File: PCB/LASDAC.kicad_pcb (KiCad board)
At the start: 2 copper layers, 110 x 70 mm, 91 parts, among them P1 USB_B, P2 CONN_01X25, U1 Mounting_Hole, U10 TL084_v, U11 LM358, U12 TL084_v, U2 Mounting_Hole, U3 Mounting_Hole, U4 Mounting_Hole, U5 AP2114, U6 SPX431, U7 ISA_DC-DC_converter, U8 ATSAM4S, U9 DAC084S085C, Y1 12MHz .25%

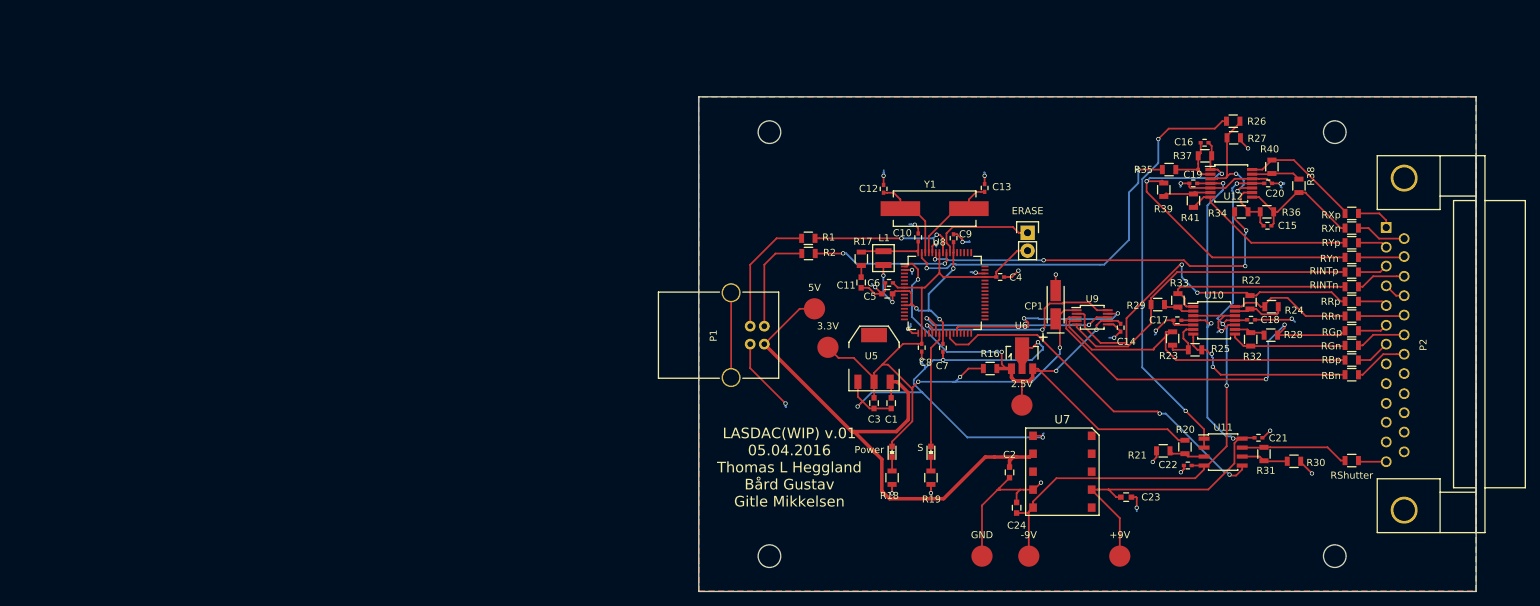
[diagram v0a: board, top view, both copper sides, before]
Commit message: Generated BOM, fixed component names in schematic
Changed component names on output resistors and status LED to match that
in PCB
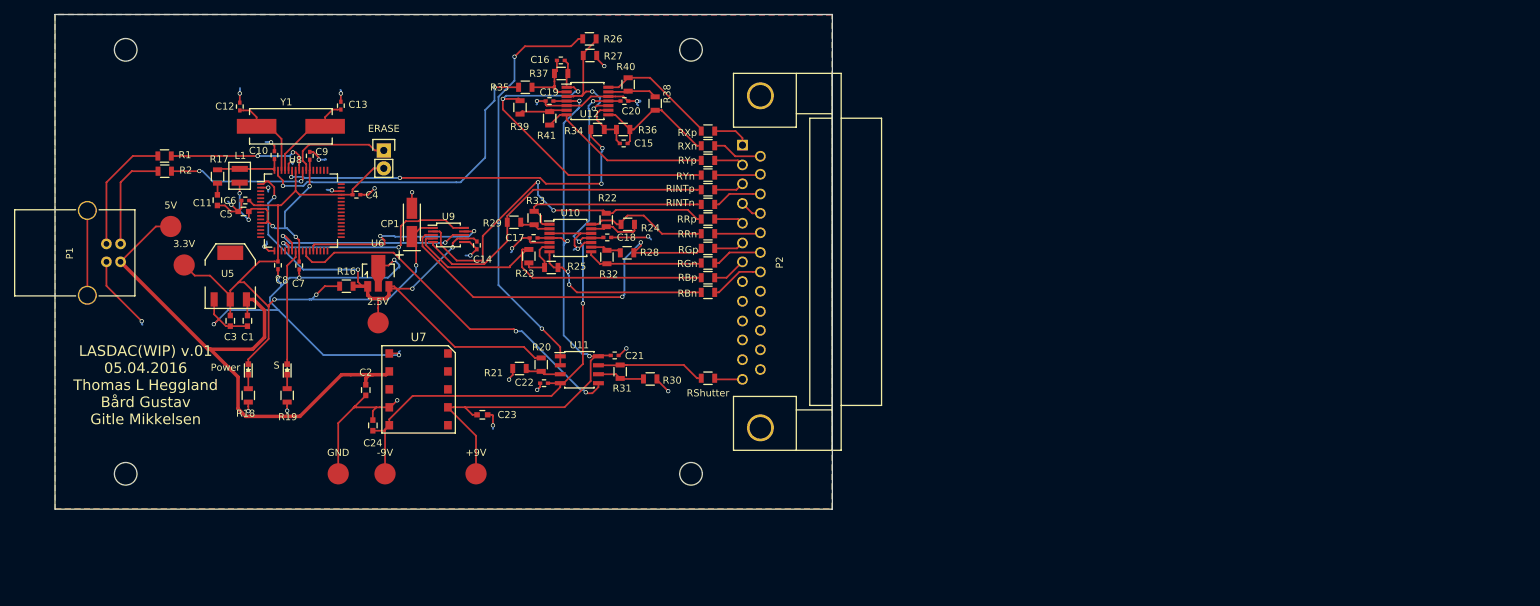
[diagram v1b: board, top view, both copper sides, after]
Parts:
- moved P2 91.8 mm to (167.4, 83.3)
- moved R20 91.8 mm to (137.7, 97.9)
- moved R23 91.8 mm to (135.9, 82.5)
- moved R24 91.8 mm to (149.9, 78.0)
- moved R33 91.8 mm to (136.7, 77.2)
- moved R35 91.8 mm to (135.4, 58.6)
- moved R38 91.8 mm to (153.8, 61.0)
- moved R39 91.8 mm to (134.7, 61.5)
- moved U10 91.8 mm to (141.8, 80.0)
- moved 3.3V 91.8 mm to (87.2, 83.8)
- moved C10 91.8 mm to (100.0, 68.2)
- moved C12 91.8 mm to (95.0, 61.4)
- moved C3 91.8 mm to (93.7, 91.7)
- moved C4 91.8 mm to (111.5, 73.8)
- moved C5 91.8 mm to (95.6, 76.2)
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
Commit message: Reannotated Components
Annotated components to standards,
TODO: Add Silkscreen for signals on bottom
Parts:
- R16: value 1R -> 330R
- renumbered +9V to +9V1, -9V to -9V1, 2.5V to 2.5V1, 3.3V to 3.3V1, 5V to 5V1, C9 to C10, C8 to C11, C10 to C12, C11 to C13, C12 to C14, C13 to C15, C14 to C16, C15 to C17, C16 to C18, C17 to C19, C3 to C2, C18 to C20, C19 to C21, C20 to C22, C21 to C23, C22 to C24, C2 to C3, C23 to C4, C24 to C5, C5 to C6, C4 to C8, C6 to C9, Power to D1, S to D2, GND to GND1, U1 to H1, U2 to H2, U3 to H3, U4 to H4, RXn to R10, RYn to R11, RINTn to R12, RRn to R13, RGn to R14, RBn to R15, RXp to R3, R32 to R30, R33 to R31, R30 to R32, R31 to R33, RYp to R4, RINTp to R5, RRp to R6, RGp to R7, RBp to R8, RShutter to R9, U5 to U1, U6 to U2, U7 to U3, U8 to U4, U9 to U5, U10 to U6, U11 to U7, U12 to U8
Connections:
- C17 pad 2: Net-(C15-Pad2) -> Net-(C17-Pad2)
- R26 pad 1: /Amplifiers/Offset -> Net-(R26-Pad1)
- R26 pad 2: /Amplifiers/1.25V -> /Amplifiers/Offset
- R27 pad 1: /Amplifiers/1.25V -> /Amplifiers/Offset
- R34 pad 1: Net-(C15-Pad2) -> Net-(C17-Pad2)
- R36 pad 2: Net-(C15-Pad2) -> Net-(C17-Pad2)
- U6 pad 1: /Amplifiers/-Intensity -> /Amplifiers/-R
- U6 pad 13: Net-(R22-Pad1) -> Net-(R29-Pad1)
- U6 pad 14: /Amplifiers/-R -> /Amplifiers/-Intensity
- U6 pad 2: Net-(R29-Pad1) -> Net-(R22-Pad1)
- U7 pad 1: /Amplifiers/Offset -> Net-(R26-Pad1)
- U7 pad 2: /Amplifiers/Offset -> Net-(R26-Pad1)
- U8 pad 10: /Amplifiers/1.25V -> GND
- U8 pad 13: Net-(R38-Pad1) -> Net-(R39-Pad1)
- U8 pad 14: /Amplifiers/+X -> /Amplifiers/+Y
- U8 pad 3: /Amplifiers/1.25V -> /Amplifiers/Offset
- U8 pad 5: GND -> /Amplifiers/Offset
- U8 pad 6: Net-(R39-Pad1) -> Net-(C17-Pad2)
- U8 pad 7: /Amplifiers/+Y -> /Amplifiers/-X
- U8 pad 8: /Amplifiers/-X -> /Amplifiers/+X
- U8 pad 9: Net-(C15-Pad2) -> Net-(R38-Pad1)
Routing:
- net Net-(R26-Pad1): track 0.00 -> 58.9 mm, vias 0 -> 2
- net /Amplifiers/Offset: track 58.9 -> 23.1 mm
- net /Amplifiers/-X: track 19.7 -> 41.0 mm
- net /Amplifiers/+Y: track 25.1 -> 4.30 mm
- net /Amplifiers/1.25V: track 18.4 -> 0.00 mm, vias 2 -> 0
- net Net-(C15-Pad2): track 8.42 -> 0.00 mm
- net Net-(C17-Pad2): track 0.00 -> 7.24 mm
- net GND: track 192.6 -> 187.9 mm
- net Net-(R39-Pad1): track 6.83 -> 9.53 mm
- net Net-(R38-Pad1): track 7.00 -> 5.47 mm
- net /Amplifiers/-R: track 18.3 -> 17.4 mm
- net /Amplifiers/-Intensity: track 27.9 -> 28.8 mm

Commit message: Replaced L1 footprint, changed Resistor values
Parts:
- removed R17: 1R, Resistors_SMD:R_0805
- L1: footprint Personal Library:Inductor_SM_1008i2520m -> Resistors_SMD:R_0805
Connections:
- C13 pad 1: Net-(C13-Pad1) -> /Microcontroller/VDDPLL
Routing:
- net GND: track 187.9 -> 191.8 mm, vias 32 -> 33
- net /Amplifiers/Offset: track 23.1 -> 19.2 mm, vias 2 -> 1
- net /Amplifiers/-R: track 17.4 -> 14.7 mm
- net /Amplifiers/-Intensity: track 28.8 -> 31.5 mm
- net /Microcontroller/VDDPLL: track 9.78 -> 11.8 mm
- net Net-(C13-Pad1): track 1.66 -> 0.00 mm
- net Net-(R38-Pad1): track 5.47 -> 7.03 mm
- net Net-(C17-Pad2): track 7.24 -> 5.68 mm

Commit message: Fixed schematic errors, "small" changes to PCB
Flipped DAC, changed component values, removed 1 capacitor, moved c16
from vref to power. Developed an urge to kill kicad
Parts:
- removed the C2 at (93.7, 91.7)
- C14, C15: value C -> 13pF
- C6: value 2.2uF -> 4.7uF
- R16: value 330R -> 150R
- R18, R19: value 330R -> 1.65k
- R33: value 10k -> 5.11k
- moved C2 29.4 mm to (90.9, 85.0)
- moved U1 10.4 mm to (90.9, 95.3), turned to 180 degrees
- moved C1 9.91 mm to (86.2, 92.2)
- moved C16 3.68 mm to (125.4, 82.8)
- moved 3.3V1 2.49 mm to (85.0, 85.0)
- moved U5 1.75 mm to (122.8, 79.5), turned to 180 degrees
- renumbered CP1 to C2
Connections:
- C16 pad 1: /Amplifiers/2.5V -> /DAC/3.3V
- U5 pad 2: /Amplifiers/+R -> /Amplifiers/+G
- U5 pad 3: /Amplifiers/+G -> /Amplifiers/+B
- U5 pad 4: /Amplifiers/+B -> /Amplifiers/+Intensity
- U5 pad 5: /Amplifiers/+Intensity -> /Amplifiers/+R
- U6 pad 1: /Amplifiers/-R -> /Amplifiers/-Intensity
- U6 pad 13: Net-(R29-Pad1) -> Net-(R22-Pad1)
- U6 pad 14: /Amplifiers/-Intensity -> /Amplifiers/-R
- U6 pad 2: Net-(R22-Pad1) -> Net-(R29-Pad1)
- U8 pad 10: GND -> /Amplifiers/Offset
- U8 pad 13: Net-(R39-Pad1) -> Net-(R38-Pad1)
- U8 pad 14: /Amplifiers/+Y -> /Amplifiers/+X
- U8 pad 5: /Amplifiers/Offset -> GND
- U8 pad 6: Net-(C17-Pad2) -> Net-(R39-Pad1)
- U8 pad 7: /Amplifiers/-X -> /Amplifiers/+Y
- U8 pad 8: /Amplifiers/+X -> /Amplifiers/-X
- U8 pad 9: Net-(R38-Pad1) -> Net-(C17-Pad2)
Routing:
- net /Amplifiers/-X: track 41.0 -> 19.7 mm
- net /Amplifiers/+Y: track 4.30 -> 25.1 mm
- net GND: track 191.8 -> 177.5 mm, vias 33 -> 32
- net /Power Regulation/5V: track 81.9 -> 69.4 mm
- net /DAC/!SYNC: track 27.4 -> 16.4 mm, vias 2 -> 0
- net /DAC/SCLK: track 31.1 -> 21.9 mm
- net /Amplifiers/+R: track 51.2 -> 42.1 mm
- net /DAC/3.3V: track 105.9 -> 114.5 mm
- net /DAC/Din: track 29.3 -> 21.5 mm, vias 2 -> 0
- net /Amplifiers/+B: track 48.4 -> 41.6 mm
- net /Amplifiers/+G: track 54.6 -> 48.1 mm
- net /Amplifiers/+Intensity: track 46.0 -> 41.0 mm
- net /Amplifiers/-R: track 14.7 -> 18.3 mm
- net /Amplifiers/-Intensity: track 31.5 -> 27.9 mm
- net Net-(C17-Pad2): track 5.68 -> 8.42 mm
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
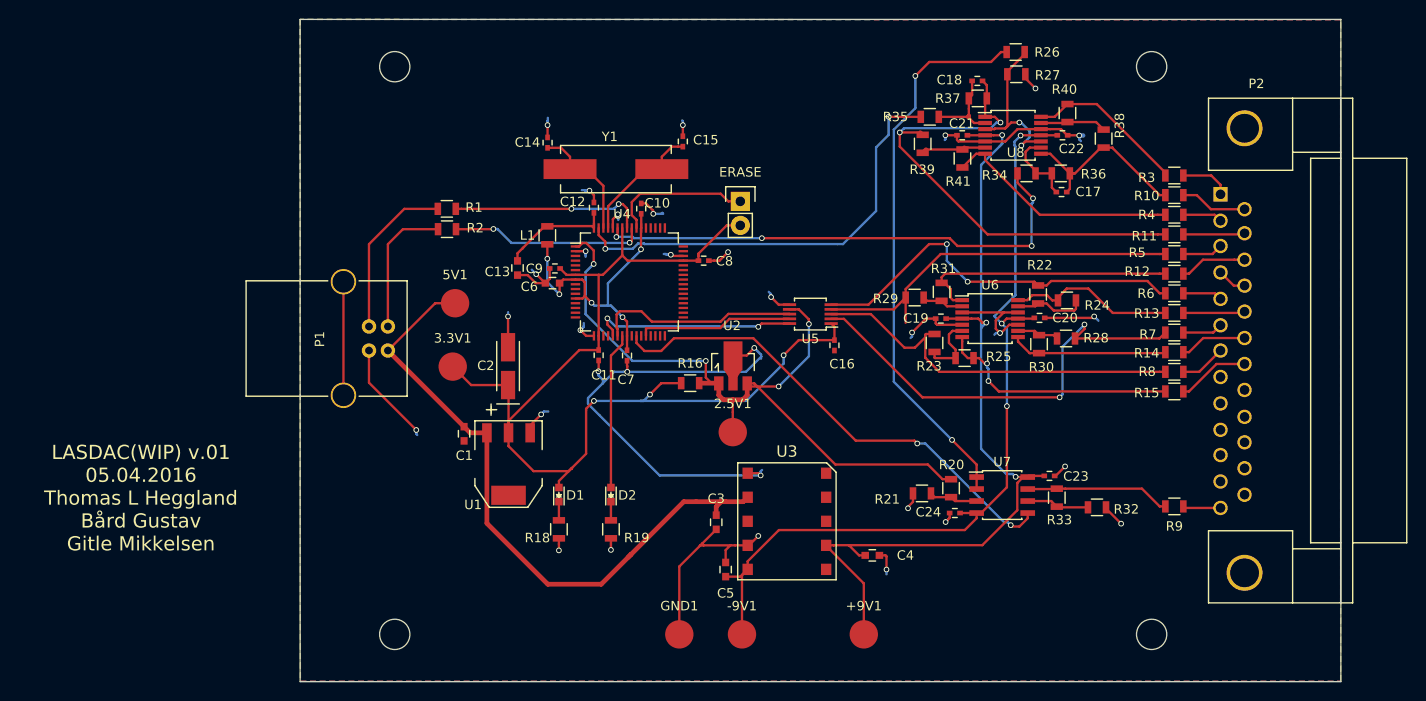
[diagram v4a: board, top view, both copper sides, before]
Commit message: Resized board
Resized board to be shorter than 100mm
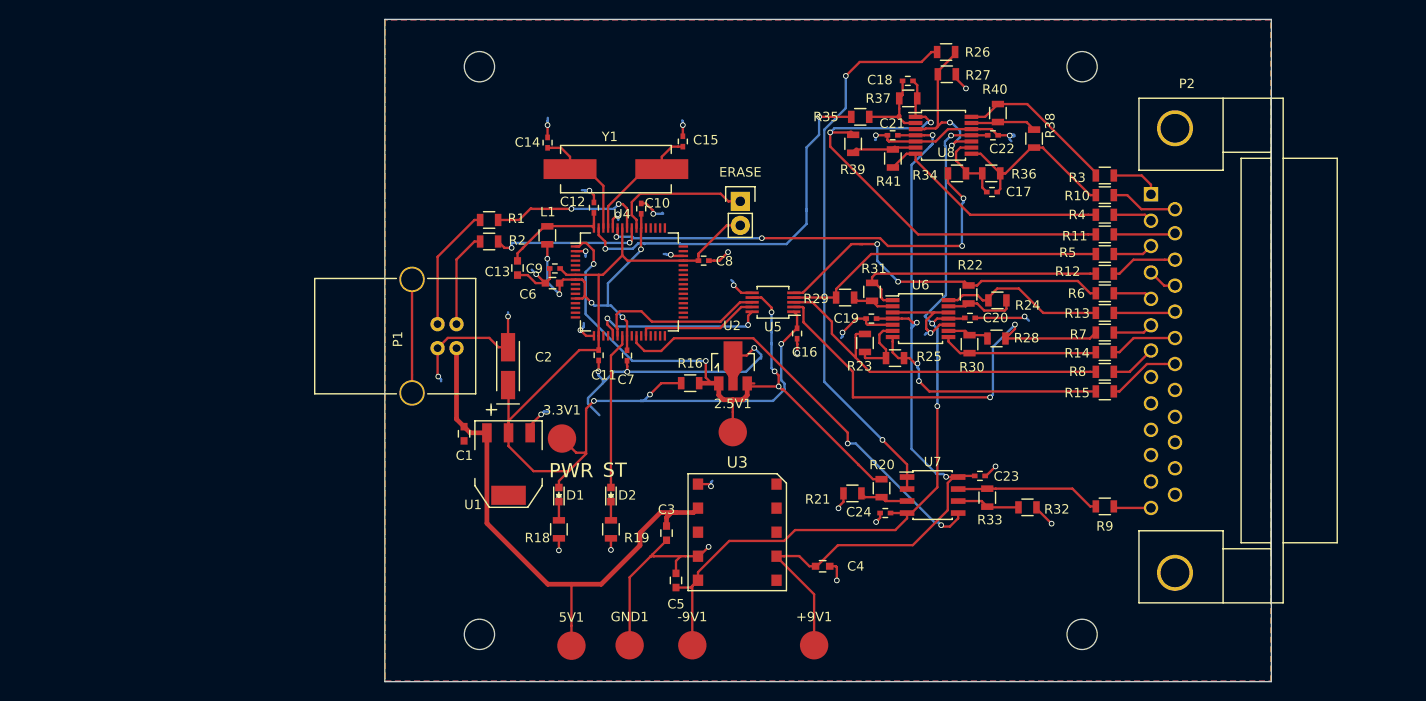
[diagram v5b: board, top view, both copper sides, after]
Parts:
- moved 5V1 38.2 mm to (97.6, 114.5)
- moved 3.3V1 13.8 mm to (96.6, 92.7)
- moved H2 8.95 mm to (87.8, 53.4)
- moved H3 8.95 mm to (87.8, 113.3)
- moved C20 7.35 mm to (139.7, 79.9)
- moved R10 7.35 mm to (153.9, 66.9)
- moved R11 7.35 mm to (153.9, 71.1)
- moved R12 7.35 mm to (153.9, 75.2)
- moved R13 7.35 mm to (153.9, 79.4)
- moved R14 7.35 mm to (153.9, 83.5)
- moved R15 7.35 mm to (153.9, 87.7)
- moved R3 7.35 mm to (153.9, 64.8)
- moved R34 7.35 mm to (138.3, 64.6)
- moved R36 7.35 mm to (141.9, 64.6)
- moved R4 7.35 mm to (153.9, 69.0)
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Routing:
- net GND: track 177.5 -> 160.1 mm, vias 32 -> 33
- net /Power Regulation/5V: track 69.4 -> 58.6 mm
- net /Amplifiers/2.5V: track 79.3 -> 69.7 mm, vias 4 -> 5
- net /Amplifiers/X: track 53.7 -> 46.4 mm
- net /Amplifiers/Shutter: track 52.2 -> 45.5 mm
- net /Amplifiers/+Intensity: track 41.0 -> 34.4 mm
- net /Amplifiers/Y: track 46.7 -> 40.5 mm
- net /D-: track 14.7 -> 10.1 mm
- net /D+: track 17.5 -> 13.2 mm
- net /Microcontroller/D-: track 20.6 -> 16.4 mm
- net /Microcontroller/D+: track 20.6 -> 16.6 mm
- net /Amplifiers/+R: track 42.1 -> 38.5 mm
- net /DAC/3.3V: track 114.5 -> 111.1 mm
- net /DAC/!SYNC: track 16.4 -> 12.9 mm
- net /DAC/Din: track 21.5 -> 18.1 mm
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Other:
- board size 110 x 70 mm -> 93.7 x 70 mm
- board text added: "PWR"
- board text added: "ST"
